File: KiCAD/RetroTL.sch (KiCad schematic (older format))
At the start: 15 parts, among them J1 Arduino_ProMini_Angeld_Header, P1 MAINS, P2 Leds, P3 Rotary, P4 0-10V, T1 NA03-T2S09/HLK-PM12, U1 G3MB, U2 LM358, U3 LM2596_mod, U4 433Mhz

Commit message: Schematic change to RF34L01
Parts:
- removed U4: 433Mhz, septillion_Modules:RM433_receiver_4pin, symbol RM433_receiver_4pin
- added C3: CP_Small, Capacitors_ThroughHole:C_Radial_D5_L6_P2.5, symbol CP_Small
- added C4: C_Small, Capacitors_SMD:C_0805_HandSoldering, symbol C_Small
- added U4: 78L33, TO_SOT_Packages_THT:TO-92_Inline_Narrow_Oval, symbol LM7805CT
- added U5: nRF24L01+, myelin-kicad:NRF24L01_MODULE, symbol nRF24L01+
- J1: footprint septillion_Arduino:arduino_pro_mini_(angle)_header -> septillion_Arduino:arduino_pro_mini_(angle)_header(RetroTL); symbol Arduino_ProMini_Angeld_Header -> Arduino_ProMini_Angeled(RetroTL)
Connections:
- net +9V: now also C3.1, U4.1 (IN)
- net GND: now also C3.2, C4.2, U4.2 (GND), U5.1 (GND)
- net at P2.1 (P1): now also J1.5 (D2); no longer J1.13 (SS/D10)
- net at R1.2: now also J1.6 (D3); no longer J1.14 (MOSI/D11)
- net MISO: now reaches J1.15 (MISO/D12)
- net MISO: now also U5.7 (MISO)
- net SCK: now reaches J1.16 (SCK/D13)
- net SCK: now also U5.5 (SCK)
- new net: C4.1, U4.3 (OUT), U5.2 (VCC)
- new net CE: J1.7 (D4), U5.3 (CE)
- new net CSN: J1.13 (SS/D10), U5.4 (CSN)
- new net MOSI: J1.14 (MOSI/D11), U5.6 (MOSI)
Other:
- moved on the sheet: P3, P4

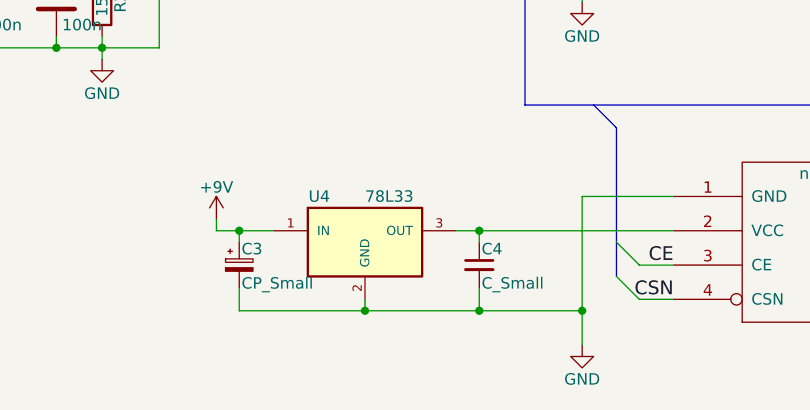
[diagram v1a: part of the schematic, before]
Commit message: Added some schematic values
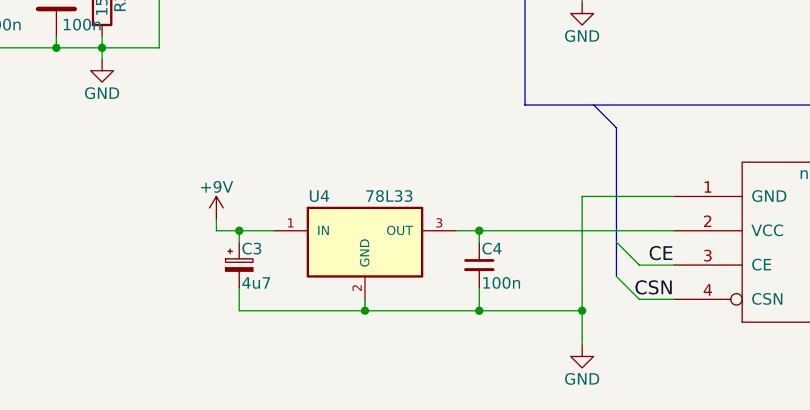
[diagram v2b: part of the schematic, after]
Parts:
- C3: value CP_Small -> 4u7
- C4: value C_Small -> 100n
- J1: footprint septillion_Arduino:arduino_pro_mini_(angle)_header(RetroTL) -> septillion_Arduino:Arduino_ProMini_Angeled_Small++
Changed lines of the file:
@@
 F 0 "J1" H 4150 2650 60  0000 C CNN
 F 1 "Arduino_ProMini_Angeld_Header" H 4200 2775 60  0000 C CNN
-F 2 "septillion_Arduino:arduino_pro_mini_(angle)_header(RetroTL)" V 4150 2650 60  0001 C CNN
+F 2 "septillion_Arduino:Arduino_ProMini_Angeled_Small++" V 4150 2650 60  0001 C CNN
 F 3 "" V 4150 2650 60  0000 C CNN
 	1    4200 2650
@@
 P 5250 5950
 F 0 "C4" H 5260 6020 50  0000 L CNN
-F 1 "C_Small" H 5260 5870 50  0000 L CNN
+F 1 "100n" H 5260 5870 50  0000 L CNN
 F 2 "Capacitors_SMD:C_0805_HandSoldering" H 5250 5950 50  0001 C CNN
 F 3 "" H 5250 5950 50  0000 C CNN
@@
 P 4200 5950
 F 0 "C3" H 4210 6020 50  0000 L CNN
-F 1 "CP_Small" H 4210 5870 50  0000 L CNN
+F 1 "4u7" H 4210 5870 50  0000 L CNN
 F 2 "Capacitors_ThroughHole:C_Radial_D5_L6_P2.5" H 4200 5950 50  0001 C CNN
 F 3 "" H 4200 5950 50  0000 C CNN
